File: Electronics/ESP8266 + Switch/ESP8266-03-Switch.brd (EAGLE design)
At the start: 160 x 100 mm, 10 parts, among them IC1 REG1117, J1 22-27-2021-02, J2 22-27-2031-03, J3 22-27-2031-03, J4 22-27-2031-03

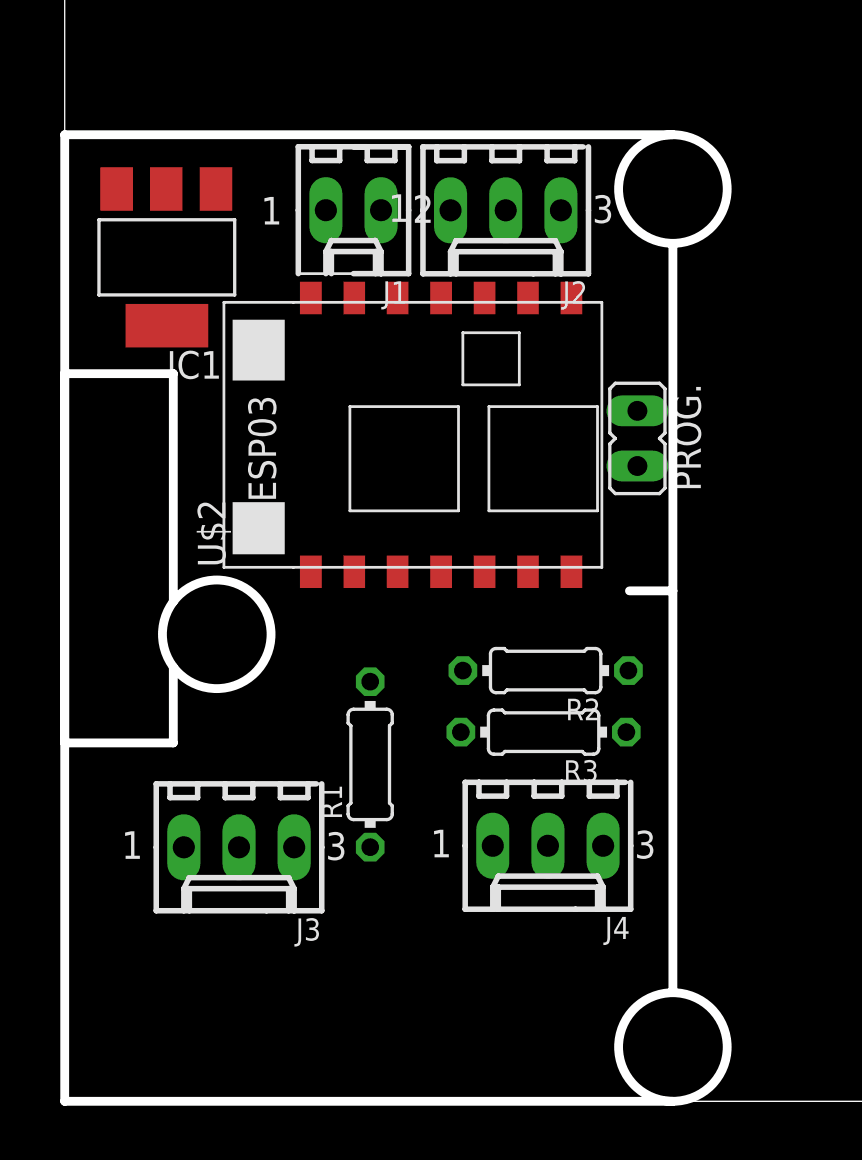
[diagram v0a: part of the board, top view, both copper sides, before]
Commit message: - new Switch and RGB boards
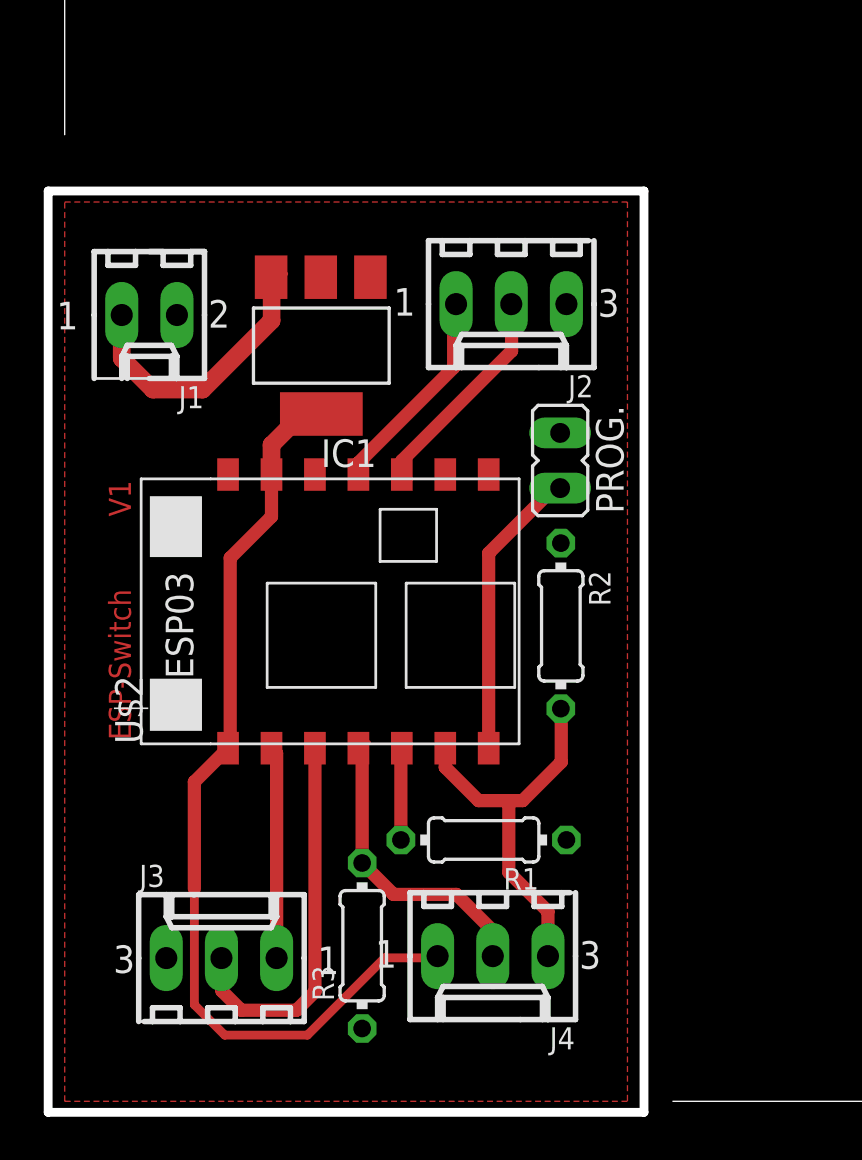
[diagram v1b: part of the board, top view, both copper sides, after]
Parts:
- moved R3 12.9 mm to (13.7, 7.16), turned to 90 degrees
- moved J1 10.6 mm to (3.90, 36.2)
- moved U$2 8.98 mm to (12.3, 21.5)
- moved IC1 8.19 mm to (11.8, 34.8)
- moved R1 6.28 mm to (19.3, 12.0), turned to 180 degrees
- moved J4 5.68 mm to (19.7, 6.68)
- moved J3 5.16 mm to (7.22, 6.59), turned to 0 degrees
- moved J2 4.33 mm to (20.6, 36.7)
- moved PROG. 3.70 mm to (22.8, 29.5)
- moved R2 2.17 mm to (22.8, 21.9), turned to 270 degrees
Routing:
- net +3V3: track 0.00 -> 42.7 mm
- net IN_2: track 0.00 -> 18.0 mm
- net RELAY_2: track 0.00 -> 17.7 mm
- net IN_1: track 0.00 -> 14.3 mm
- net N$2: track 0.00 -> 13.6 mm
- net N$1: track 0.00 -> 13.5 mm
- net N$4: track 0.00 -> 9.95 mm
- net RELAY_1: track 0.00 -> 9.76 mm
- net N$3: track 0.00 -> 9.71 mm
- net N$6: track 0.00 -> 4.62 mm
- added copper zone on layer 1, net GND
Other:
- board size 160 x 100 mm -> 160.8 x 100.5 mm
- board text added: "ESP-Switch"
- board text added: "V1"
